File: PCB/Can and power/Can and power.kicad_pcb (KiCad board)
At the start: 2 copper layers, 37.5 x 35 mm, 32 parts, among them IC1 MCP2515-e_ST, IC2 TJA1044VT_3Z, J1 TPS54232DR, J2 ESP32, J3 12V, J4 C_H, J5 C_L, J6 GND, Y1 16MHz

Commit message: Pre-traces
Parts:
- moved C5 31.8 mm to (144.6, 101.0), turned to 180 degrees
- moved IC2 22.1 mm to (144.6, 105.8), turned to -90 degrees
- moved C4 22.0 mm to (140.0, 107.1), turned to 180 degrees
- moved J4 20.7 mm to (139.0, 115.0)
- moved J5 20.5 mm to (143.0, 115.0)
- moved D1 19.3 mm to (139.5, 112.2), turned to 180 degrees
- moved C3 19.0 mm to (140.0, 108.9), turned to 0 degrees
- moved D2 13.3 mm to (146.9, 114.5), turned to 30 degrees
- moved R8 12.9 mm to (146.6, 110.7), turned to 0 degrees
- moved R1 11.9 mm to (143.3, 110.7), turned to 0 degrees
- moved J6 10.7 mm to (126.5, 106.3), turned to 90 degrees
- moved C9 5.89 mm to (127.6, 111.2), turned to 135 degrees
- moved C10 5.57 mm to (132.4, 98.2), turned to 90 degrees
- moved J3 5.57 mm to (132.6, 111.7)
- moved R4 3.94 mm to (134.9, 98.7), turned to 0 degrees
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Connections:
- C7 pad 1: Net-(C7-Pad1) -> Net-(J1-COMP)
- C7 pad 2: GND -> Net-(C7-Pad2)
- R4 pad 1: Net-(C7-Pad1) -> GND
- R4 pad 2: Net-(J1-COMP) -> Net-(C7-Pad2)

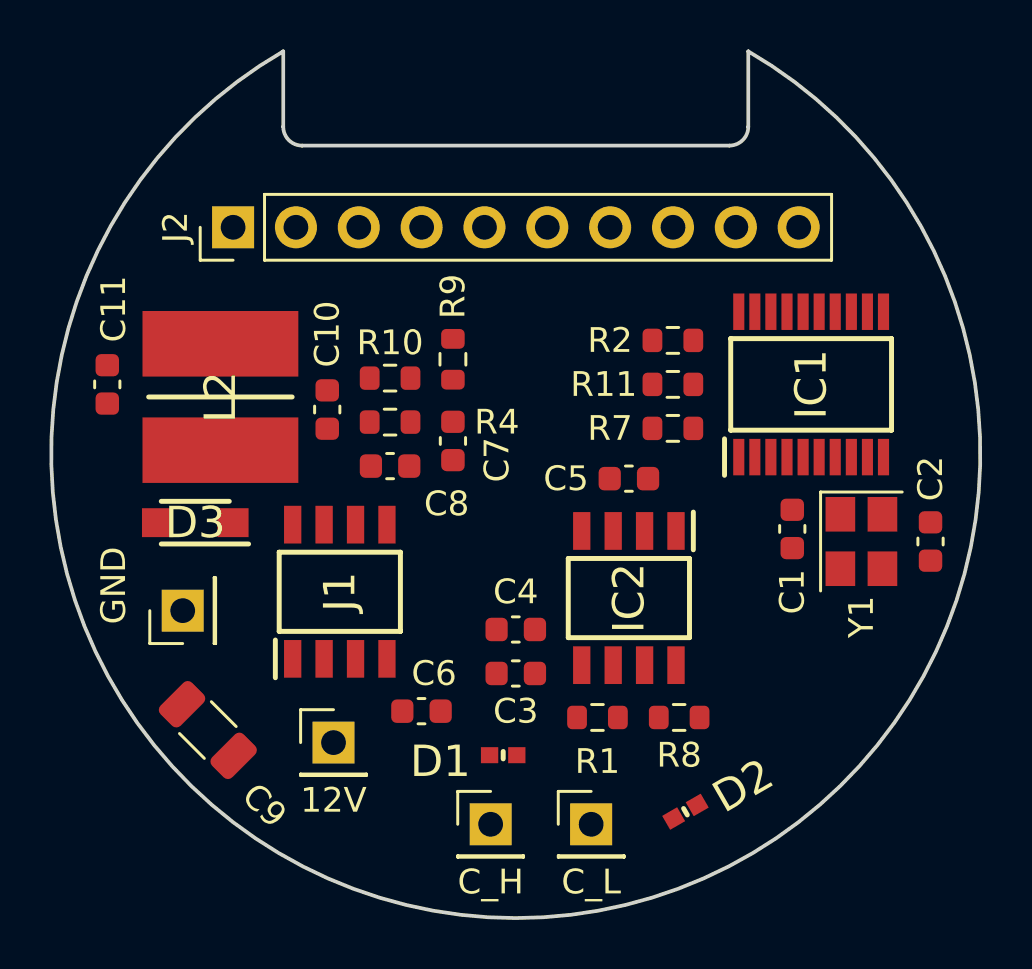
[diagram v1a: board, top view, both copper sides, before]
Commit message: First PCBWay quotation
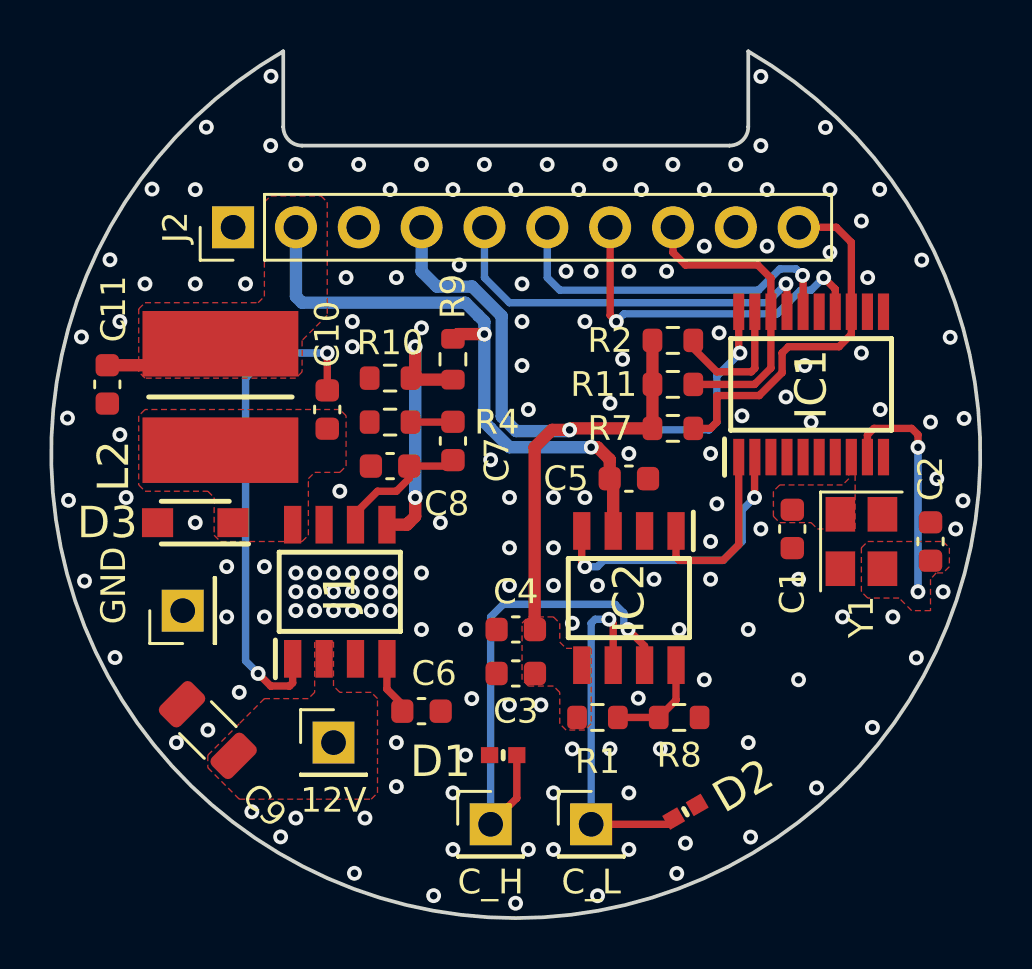
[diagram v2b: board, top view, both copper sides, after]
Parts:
- added G***: LOGO, LOGO, B.Cu at (143.8, 102.0)
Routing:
- net +3V3: track 0.00 -> 39.8 mm, vias 0 -> 2
- net VSYS: track 0.00 -> 29.8 mm, vias 0 -> 2
- net Net-(J1-BOOT): track 0.00 -> 20.0 mm, vias 0 -> 2
- net Net-(IC2-CANH): track 0.00 -> 19.8 mm, vias 0 -> 1
- net GPIO15: track 0.00 -> 16.1 mm, vias 0 -> 1
- net GPIO33: track 0.00 -> 15.2 mm
- net GPIO17: track 0.00 -> 14.6 mm, vias 0 -> 2
- net GPIO16: track 0.00 -> 14.5 mm, vias 0 -> 1
- net Net-(IC2-CANL): track 0.00 -> 14.3 mm, vias 0 -> 1
- net GPIO18: track 0.00 -> 12.5 mm
- net RX_CAN: track 0.00 -> 11.9 mm, vias 0 -> 2
- net Net-(J1-VSENSE): track 0.00 -> 11.2 mm, vias 0 -> 2
- net Net-(IC1-OSC1): track 0.00 -> 9.50 mm, vias 0 -> 2
- net TX_CAN: track 0.00 -> 7.45 mm
- net Net-(J1-COMP): track 0.00 -> 5.58 mm
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- added copper zone on F.Cu, net +12V
- added copper zone on F.Cu, net +3V3
- added copper zone on B.Cu, net GND
- added copper zone on F.Cu, net GND
- added copper zone on F.Cu, net Net-(IC1-OSC1)
- added copper zone on F.Cu, net Net-(IC1-OSC2)
- added copper zone on F.Cu, net Net-(J1-PH)
- added copper zone on F.Cu, net VSYS
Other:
- board text added: "12V"
- board text added: "15"
- board text added: "16"
- board text added: "17"
- board text added: "18"
- board text added: "21"
- board text added: "33"
- board text added: "3v3"
- board text added: "5V"
- board text added: "CAN_H"
- board text added: "CAN_L"
- board text added: "GND"
- board text added: "MRR"
- board text added: "WAYWAYWAY"
- board text added: "rev0"

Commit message: First purchase
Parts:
- C10, C3, C4, C5: value 100n -> 0.1uF
- C11: value 10u -> 10uF
- C6: value 8n2 -> 8200pF
- C7: value 4n7 -> 4700pF
- C8: value 110p -> 100pF

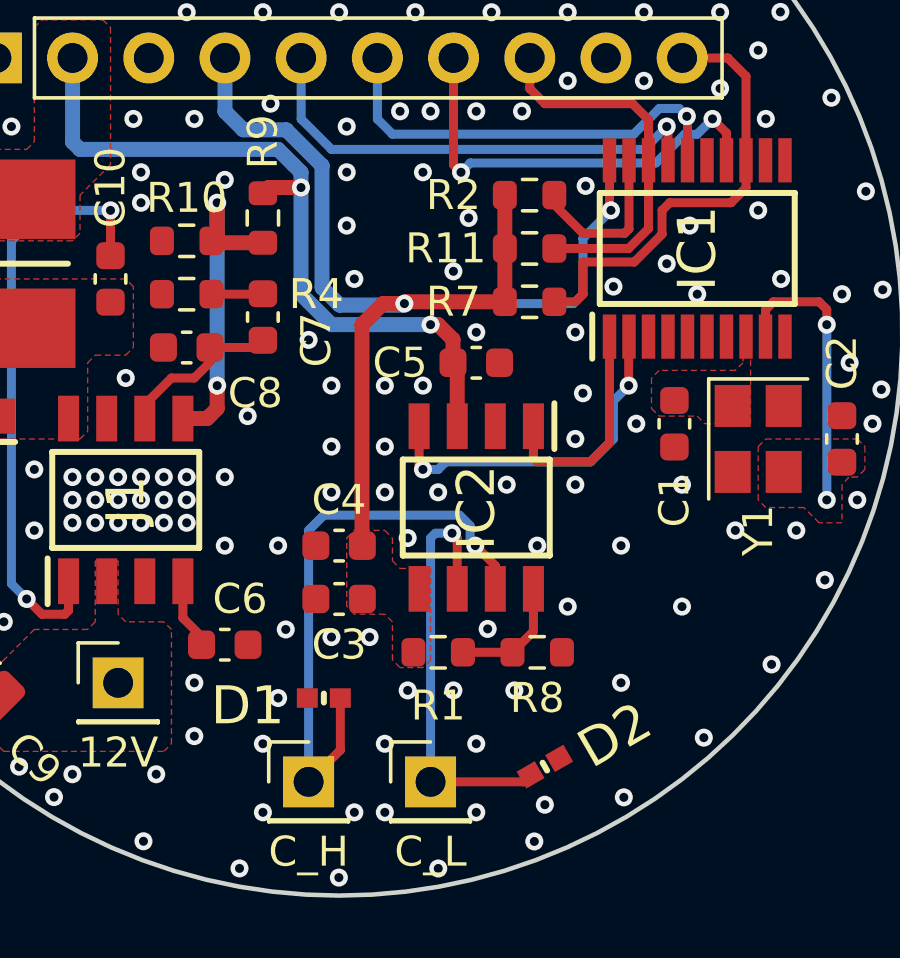
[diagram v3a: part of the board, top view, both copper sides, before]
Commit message: Change of transceiver
For some reasons the TJA 1044 and 1049 get stuck in Standby mode all the time. Not sure why.
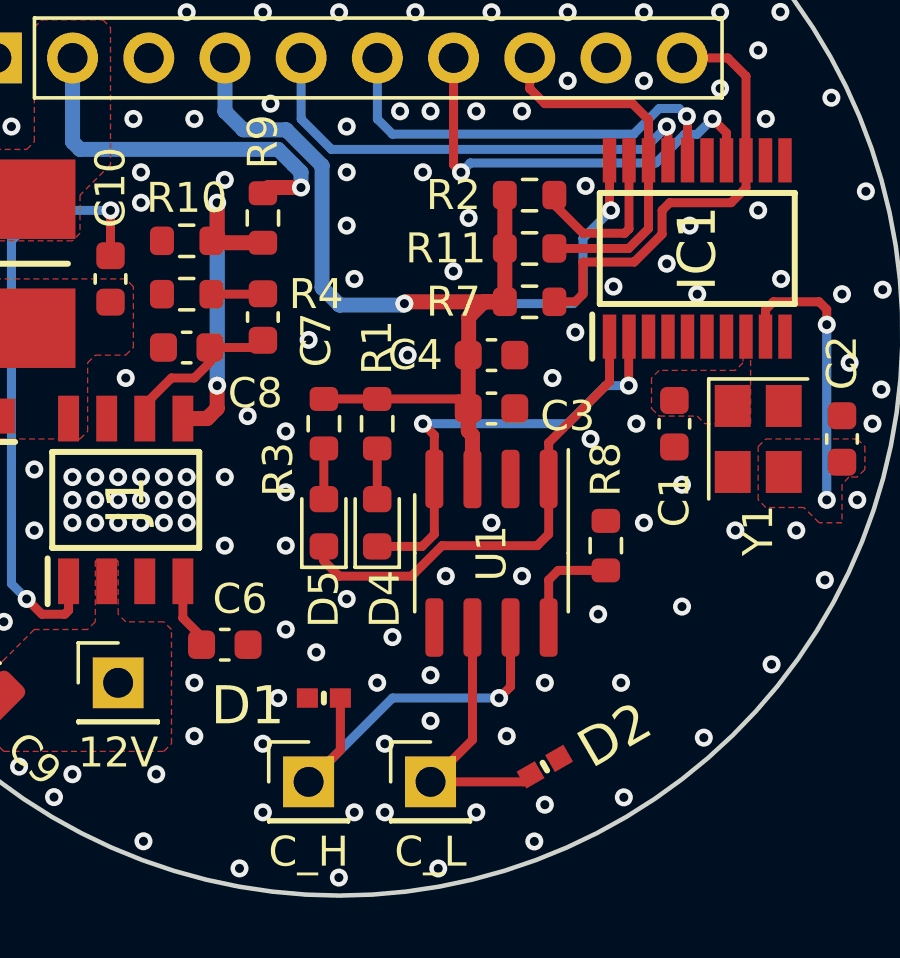
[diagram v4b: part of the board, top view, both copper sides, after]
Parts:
- removed C5: 0.1uF, Capacitor_SMD:C_0603_1608Metric
- removed IC2: TJA1044VT_3Z, SamacSys_Parts:SOIC127P600X175-8N
- added D4: 2V-20mA, LED_SMD:LED_0603_1608Metric, F.Cu at (141.3, 106.3)
- added D5: 2V - 20mA, LED_SMD:LED_0603_1608Metric, F.Cu at (139.5, 106.3)
- added R3: 68, Resistor_SMD:R_0603_1608Metric, F.Cu at (139.5, 103.0)
- added U1: SN65HVD230, Package_SO:SOIC-8_3.9x4.9mm_P1.27mm, F.Cu at (145.1, 107.4)
- R1: value 10k2 -> 68
- R8: value 0 -> 47k
- moved C3 8.13 mm to (145.1, 102.5), turned to 180 degrees
- moved C4 8.13 mm to (145.1, 100.8), turned to 0 degrees
- moved R1 7.89 mm to (141.3, 103.0), turned to 90 degrees
- moved R8 4.23 mm to (148.9, 107.1), turned to 90 degrees
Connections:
- R1 pad 1: +3V3 -> Net-(D4-A)
- R1 pad 2: Net-(IC2-STB) -> +3V3
- R8 pad 1: Net-(IC2-STB) -> Net-(U1-Rs)
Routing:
- net VSYS: track 29.8 -> 17.6 mm, vias 2 -> 1
- net TX_CAN: track 7.45 -> 16.2 mm
- net Net-(J4-Pin_1): track 19.8 -> 13.2 mm
- net Net-(J5-Pin_1): track 14.3 -> 9.15 mm, vias 1 -> 0
- net Net-(IC2-STB): track 4.06 -> 0.00 mm
- net Net-(U1-Rs): track 0.00 -> 3.62 mm
- net RX_CAN: track 11.9 -> 14.9 mm
- net +3V3: track 39.8 -> 42.5 mm
- net Net-(D5-A): track 0.00 -> 1.69 mm
- net Net-(D4-A): track 0.00 -> 1.69 mm
- net GND: vias 161 -> 155
- removed copper zone on F.Cu, net +3V3
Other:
- board text added: "rev1"
- board text removed: "rev0"

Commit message: LED resistor corrections
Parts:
- R1, R3: value 68 -> 1k
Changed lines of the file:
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@@
     (descr "Resistor SMD 0603 (1608 Metric), square (rectangular) end terminal, IPC_7351 nominal, (Body size source: IPC-SM-782 page 72, https://www.pcb-3d.com/wordpress/wp-content/uploads/ipc-sm-782a_amendment_1_and_2.pdf), generated with kicad-footprint-generator")
     (tags "resistor")
-    (property "Description" "RES 68 OHM 1% 1/10W 0603")
+    (property "Description" "RES 1K OHM 1% 1/10W 0603")
     (property "Manufacturer_Name" "YAGEO")
-    (property "Manufacturer_Part_Number" "RC0603FR-0768RL")
+    (property "Manufacturer_Part_Number" "RC0603FR-071KL")
     (property "Sheetfile" "Can and power.kicad_sch")
     (property "Sheetname" "")
@@
         (effects (font (size 1 1) (thickness 0.15)))
     )
-    (fp_text value "68" (at 0 1.43 90) (layer "F.Fab")
+    (fp_text value "1k" (at 0 1.43 90) (layer "F.Fab")
         (effects (font (size 1 1) (thickness 0.15)))
     )
@@
     (descr "Resistor SMD 0603 (1608 Metric), square (rectangular) end terminal, IPC_7351 nominal, (Body size source: IPC-SM-782 page 72, https://www.pcb-3d.com/wordpress/wp-content/uploads/ipc-sm-782a_amendment_1_and_2.pdf), generated with kicad-footprint-generator")
     (tags "resistor")
-    (property "Description" "RES 68 OHM 1% 1/10W 0603")
+    (property "Description" "RES 1K OHM 1% 1/10W 0603")
     (property "Manufacturer_Name" "YAGEO")
-    (property "Manufacturer_Part_Number" "RC0603FR-0768RL")
+    (property "Manufacturer_Part_Number" "RC0603FR-071KL")
     (property "Sheetfile" "Can and power.kicad_sch")
     (property "Sheetname" "")
@@
         (effects (font (size 1 1) (thickness 0.15)))
     )
-    (fp_text value "68" (at 0 1.43 90) (layer "F.Fab")
-        (effects (font (size 1 1) (thickness 0.15)))
-    )
+    (fp_text value "1k" (at 0 1.43 90) (layer "F.Fab")
+        (effects (font (size 1 1) (thickness 0.15)))
+    )

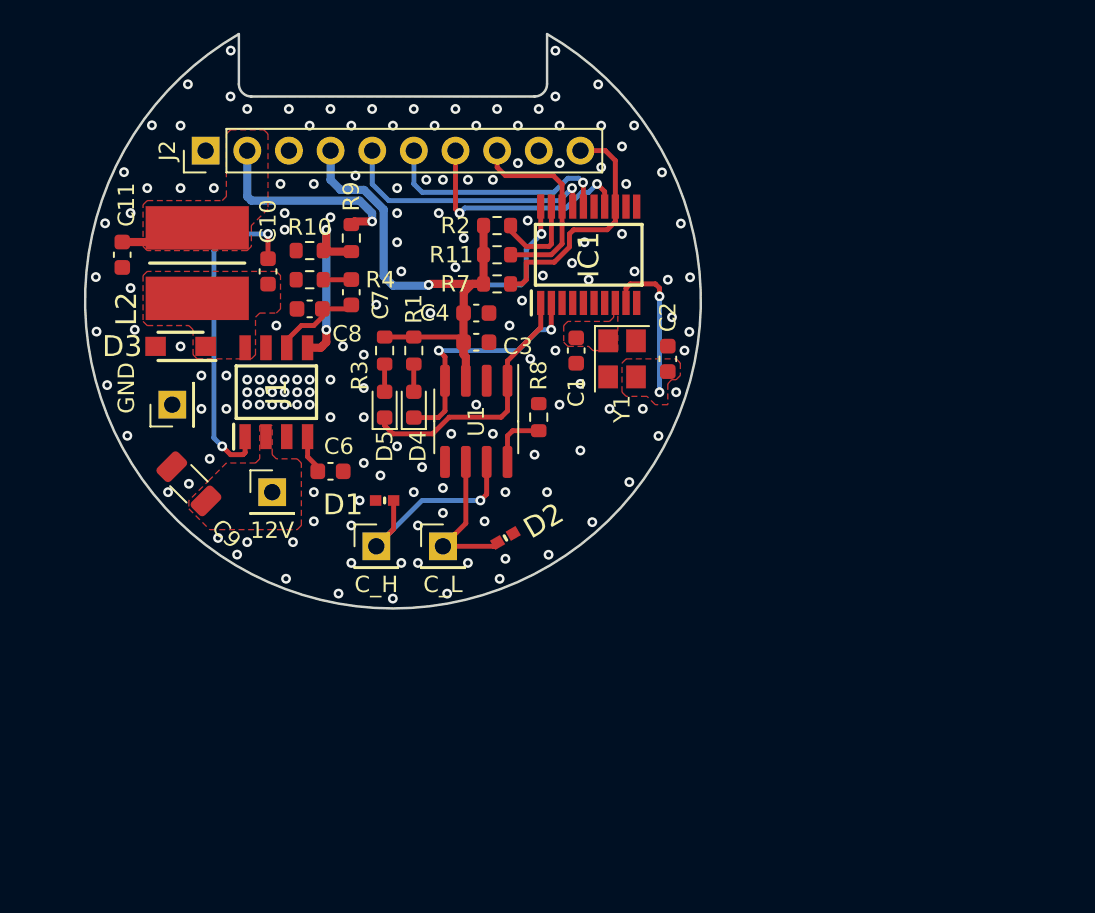
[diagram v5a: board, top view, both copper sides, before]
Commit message: Clean-up code and sch, PCB layout is a WIP
Code limited to TWAI implementation
Schematic updated with solder bridges
PCB layout is a WIP
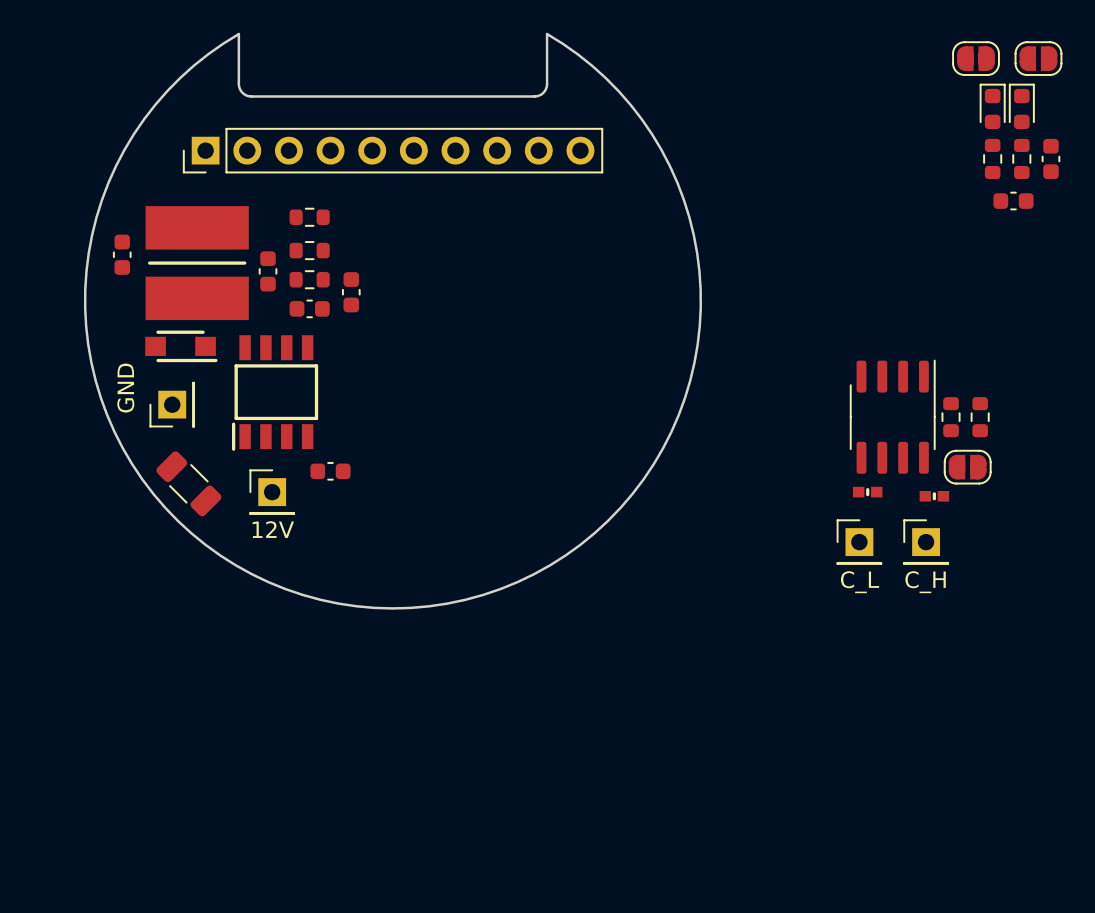
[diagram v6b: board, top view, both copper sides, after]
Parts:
- removed C1, C2: 22pF, Capacitor_SMD:C_0603_1608Metric
- removed IC1: MCP2515-e_ST, SamacSys_Parts:SOP65P640X120-20N
- removed R11, R7: 10k2, Resistor_SMD:R_0603_1608Metric
- removed Y1: 16MHz, Crystal:Crystal_SMD_3225-4Pin_3.2x2.5mm
- added JP1: SolderJumper_2_Open, Jumper:SolderJumper-2_P1.3mm_Open_RoundedPad1.0x1.5mm, F.Cu at (175.1, 110.2)
- added JP2: SolderJumper_2_Open, Jumper:SolderJumper-2_P1.3mm_Open_RoundedPad1.0x1.5mm, F.Cu at (179.4, 85.2)
- added JP3: SolderJumper_2_Open, Jumper:SolderJumper-2_P1.3mm_Open_RoundedPad1.0x1.5mm, F.Cu at (175.6, 85.2)
- R2: value 10k2 -> 1k
- moved D4 41.2 mm to (178.4, 88.3), turned to -90 degrees
- moved D5 41.2 mm to (176.6, 88.3), turned to -90 degrees
- moved R3 40.6 mm to (178.4, 91.4), turned to 90 degrees
- moved R1 37.2 mm to (176.6, 91.4), turned to -90 degrees
- moved C4 36.3 mm to (180.1, 91.4), turned to 90 degrees
- moved C3 33.9 mm to (177.8, 93.9)
- moved D1 33.5 mm to (173.0, 111.9), turned to 0 degrees
- moved J4 33.5 mm to (172.5, 114.7)
- moved R2 31.7 mm to (175.8, 107.1), turned to 90 degrees
- moved J5 25.4 mm to (168.4, 114.7)
- moved U1 25.4 mm to (170.5, 107.1)
- moved R8 25.1 mm to (174.0, 107.1)
- moved D2 22.3 mm to (169.0, 111.7), turned to 180 degrees
- moved R9 2.84 mm to (134.9, 94.9), turned to 180 degrees
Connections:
- D4 pad 1: RX_CAN -> Net-(D4-K)
- D5 pad 1: TX_CAN -> Net-(D5-K)
- R2 pad 2: +3V3 -> GND
- U1 pad 1: TX_CAN -> GPIO15
- U1 pad 4: RX_CAN -> GPIO16
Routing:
- net +3V3: track 42.5 -> 0.00 mm, vias 2 -> 0
- net Net-(J1-BOOT): track 20.0 -> 0.00 mm, vias 2 -> 0
- net VSYS: track 17.6 -> 0.00 mm, vias 1 -> 0
- net TX_CAN: track 16.2 -> 0.00 mm
- net GPIO15: track 16.1 -> 0.00 mm, vias 1 -> 0
- net GPIO33: track 15.2 -> 0.00 mm
- net RX_CAN: track 14.9 -> 0.00 mm, vias 2 -> 0
- net GPIO17: track 14.6 -> 0.00 mm, vias 2 -> 0
- net GPIO16: track 14.5 -> 0.00 mm, vias 1 -> 0
- net Net-(J4-Pin_1): track 13.2 -> 0.00 mm, vias 1 -> 0
- net GPIO18: track 12.5 -> 0.00 mm
- net Net-(J1-VSENSE): track 11.2 -> 0.00 mm, vias 2 -> 0
- net Net-(IC1-OSC1): track 9.50 -> 0.00 mm, vias 2 -> 0
- net Net-(J5-Pin_1): track 9.15 -> 0.00 mm
- net Net-(J1-COMP): track 5.58 -> 0.00 mm
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- removed copper zone on F.Cu, net +12V
- removed copper zone on F.Cu, net Net-(IC1-OSC1)
- removed copper zone on F.Cu, net Net-(IC1-OSC2)
- removed copper zone on F.Cu, net Net-(J1-PH)
- removed copper zone on F.Cu, net VSYS
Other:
- board text removed: "12V"
- board text removed: "CAN_H"
- board text removed: "CAN_L"
- board text removed: "GND"
